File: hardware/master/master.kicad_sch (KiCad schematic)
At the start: 0 parts

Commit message: Master card: DRV135 outputs, TL062 levers, SMD electrolytics, both raw rails watched (decisions 125-128)
/board master pre-layout session; the user delegated the open points.
- Confirms the [proposed] parts of decisions 89-94 (Q5 checked, +22 dB
  makeup kept for the breadboard, fallback R439 = 330k).
- 125: TI DRV135UA replaces the end-of-life THAT1646 (THAT memo
  2026-09-01); same SO-8 pinout, LCSC C544663.
- 126: U409, U410, U802, U804 TL072 -> TL062; superdiodes and U407 stay.
- 127: master electrolytics to SMD (decision 111 parts, 5.4 mm).
- 128: U707C watches -20V_RAW (22k6/100k), wired-OR with the +20 V trip.
- Würth fields on J101/J901, BAT54 LCSC C152458, G6K and header
  drawings checked, LCSC stock checked; budget 331/260 mA typical.
- parts.csv candidates for master pots and meter LEDs; lcsc_check.py
  handles MOhm.
ERC 0/0, all netlist checks 0 problems, reuse lint clean.

Co-Authored-By: Claude Opus 5.5 <noreply@anthropic.com>
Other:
- sheet Master out ports: added -20V_RAW; removed none
- sheet Power ports: added -20V_RAW; removed none
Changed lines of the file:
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@@
+			)
+		)
+		(pin "-20V_RAW" output
+			(at 55.88 132.08 0.0000)
+			(effects
+				(font
+					(size 1.27 1.27)
+				)
+				(justify right)
 			)
 		)
@@
 				)
 				(justify left top)
+			)
+		)
+		(pin "-20V_RAW" input
+			(at 160.02 104.14 180)
+			(effects
+				(font
+					(size 1.27 1.27)
+				)
+				(justify left)
 			)
 		)
@@
 	(wire (pts (xy 55.88 96.52) (xy 60.96 96.52)) (stroke (width 0) (type default)))
 	(label "SC_SUM" (at 60.96 96.52 0) (fields_autoplaced yes) (effects (font (size 1.27 1.27)) (justify left bottom)))
+	(wire (pts (xy 55.88 132.08) (xy 60.96 132.08)) (stroke (width 0) (type default)))
+	(label "-20V_RAW" (at 60.96 132.08 0) (fields_autoplaced yes) (effects (font (size 1.27 1.27)) (justify left bottom)))
 	(wire (pts (xy 55.88 129.54) (xy 60.96 129.54)) (stroke (width 0) (type default)))
 	(label "+20V_RAW" (at 60.96 129.54 0) (fields_autoplaced yes) (effects (font (size 1.27 1.27)) (justify left bottom)))
@@
 	(wire (pts (xy 160.02 73.66) (xy 154.94 73.66)) (stroke (width 0) (type default)))
 	(label "AUX2_R_SUM" (at 154.94 73.66 180) (fields_autoplaced yes) (effects (font (size 1.27 1.27)) (justify right bottom)))
+	(wire (pts (xy 160.02 104.14) (xy 154.94 104.14)) (stroke (width 0) (type default)))
+	(label "-20V_RAW" (at 154.94 104.14 180) (fields_autoplaced yes) (effects (font (size 1.27 1.27)) (justify right bottom)))
 	(wire (pts (xy 160.02 96.52) (xy 154.94 96.52)) (stroke (width 0) (type default)))
 	(label "+20V_RAW" (at 154.94 96.52 180) (fields_autoplaced yes) (effects (font (size 1.27 1.27)) (justify right bottom)))

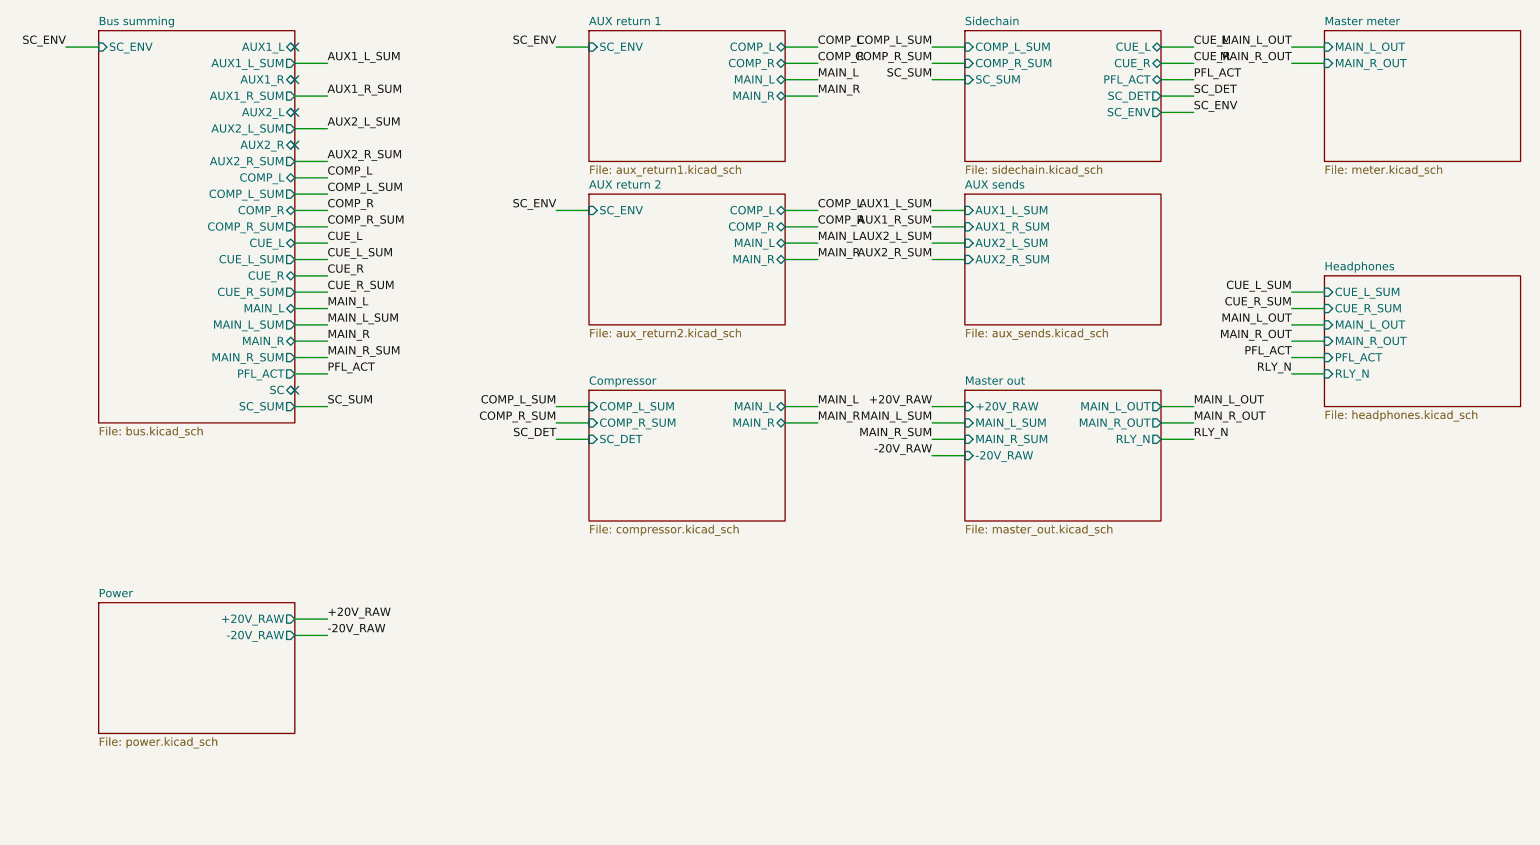
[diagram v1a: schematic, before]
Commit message: Master: rear jacks on two 26-pin row-board ribbons (decision 163)
J603 (AUX sends sheet) carries main outs and both AUX sends to the
output row board; J903 (Power sheet) brings the AUX returns, SC EXT
and the ground-lift switch (pins 25/26) from the input row board.
Pairs with a ground between them; row boards hold only jacks, header
and SW901. Netlist checks 0 problems, ERC 0/0.

Co-Authored-By: Claude Opus 5.5 <noreply@anthropic.com>
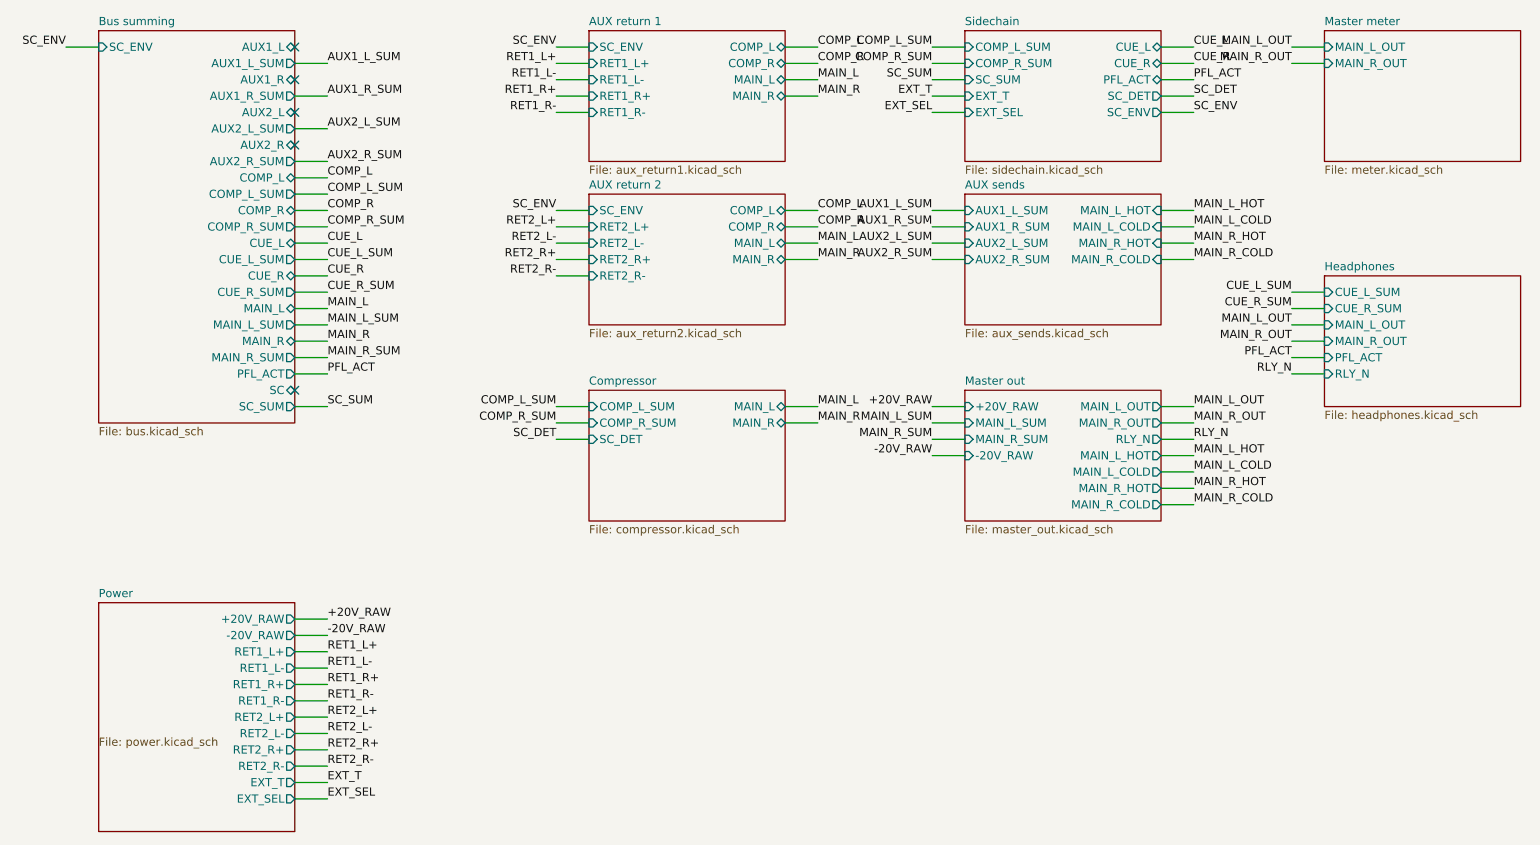
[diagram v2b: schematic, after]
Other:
- sheet AUX return 1 ports: added RET1_L+, RET1_L-, RET1_R+, RET1_R-; removed none
- sheet AUX return 2 ports: added RET2_L+, RET2_L-, RET2_R+, RET2_R-; removed none
- sheet AUX sends ports: added MAIN_L_COLD, MAIN_L_HOT, MAIN_R_COLD, MAIN_R_HOT; removed none
- sheet Master out ports: added MAIN_L_COLD, MAIN_L_HOT, MAIN_R_COLD, MAIN_R_HOT; removed none
- sheet Power ports: added EXT_SEL, EXT_T, RET1_L+, RET1_L-, RET1_R+, RET1_R-, RET2_L+, RET2_L-, RET2_R+, RET2_R-; removed none
- sheet Sidechain ports: added EXT_SEL, EXT_T; removed none
